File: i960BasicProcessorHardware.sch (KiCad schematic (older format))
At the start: 70 parts, among them J10 Conn_01x03, J11 Conn_01x08, J2 Conn_02x39_Odd_Even, J3 Conn_01x03, J4 Conn_02x05_Odd_Even, J5 Conn_02x05_Odd_Even, J6 Conn_02x05_Odd_Even, J7 Conn_01x06, J8 Conn_01x06, SW1 SW_Push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

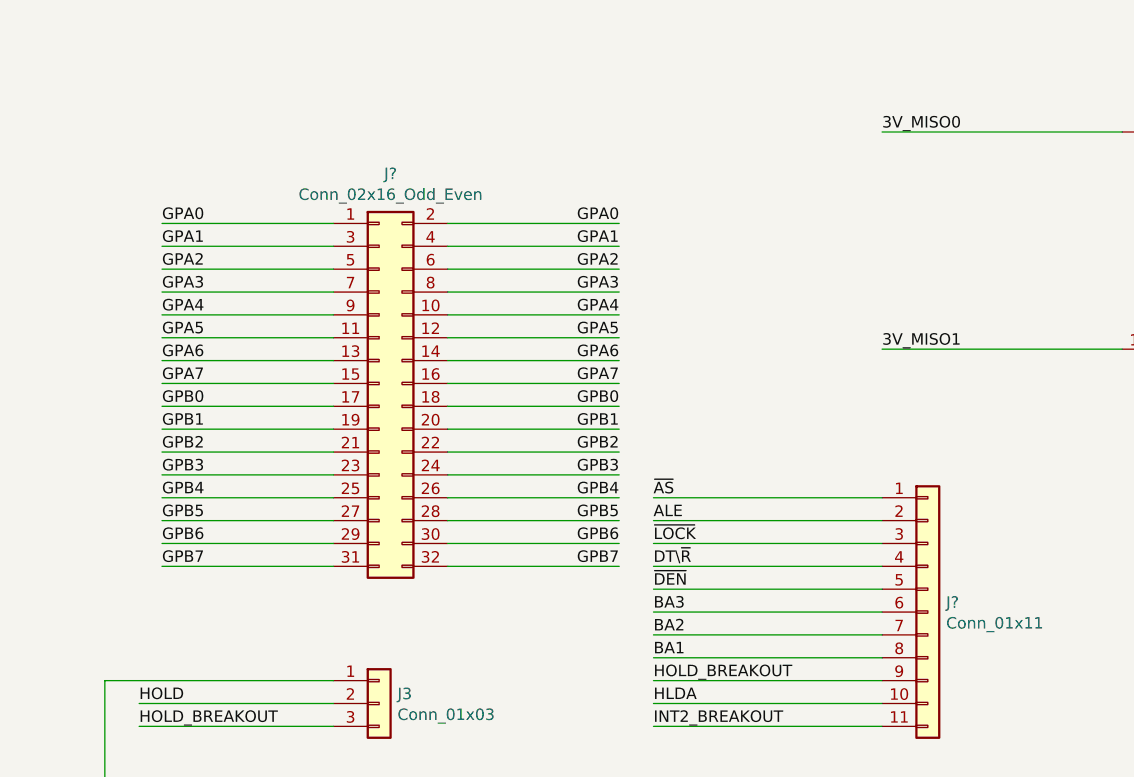
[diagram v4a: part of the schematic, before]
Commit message: Wireup the fourth gpio expander
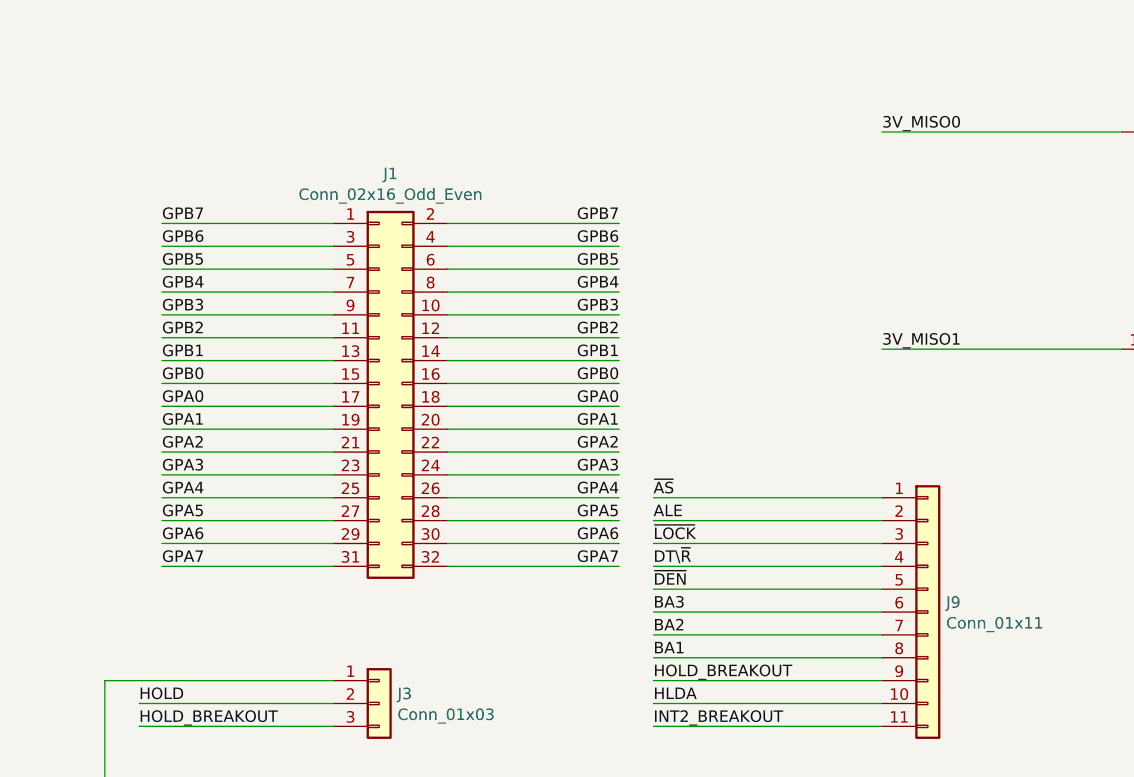
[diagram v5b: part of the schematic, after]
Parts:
- J1: renamed from J?; footprint (none) -> Connector_PinHeader_2.54mm:PinHeader_2x16_P2.54mm_Vertical
- J9: renamed from J?; footprint (none) -> Connector_PinHeader_2.54mm:PinHeader_1x11_P2.54mm_Vertical
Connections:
- net GPA0: now also J1.17 (Pin_17), J1.18 (Pin_18); no longer J1.1 (Pin_1), J1.2 (Pin_2)
- net GPA1: now also J1.19 (Pin_19), J1.20 (Pin_20); no longer J1.3 (Pin_3), J1.4 (Pin_4)
- net GPA2: now also J1.21 (Pin_21), J1.22 (Pin_22); no longer J1.5 (Pin_5), J1.6 (Pin_6)
- net GPA3: now also J1.23 (Pin_23), J1.24 (Pin_24); no longer J1.7 (Pin_7), J1.8 (Pin_8)
- net GPA4: now also J1.25 (Pin_25), J1.26 (Pin_26); no longer J1.10 (Pin_10), J1.9 (Pin_9)
- net GPA5: now also J1.27 (Pin_27), J1.28 (Pin_28); no longer J1.11 (Pin_11), J1.12 (Pin_12)
- net GPA6: now also J1.29 (Pin_29), J1.30 (Pin_30); no longer J1.13 (Pin_13), J1.14 (Pin_14)
- net GPA7: now also J1.31 (Pin_31), J1.32 (Pin_32); no longer J1.15 (Pin_15), J1.16 (Pin_16)
- net GPB0: now also J1.15 (Pin_15), J1.16 (Pin_16); no longer J1.17 (Pin_17), J1.18 (Pin_18)
- net GPB1: now also J1.13 (Pin_13), J1.14 (Pin_14); no longer J1.19 (Pin_19), J1.20 (Pin_20)
- net GPB2: now also J1.11 (Pin_11), J1.12 (Pin_12); no longer J1.21 (Pin_21), J1.22 (Pin_22)
- net GPB3: now also J1.10 (Pin_10), J1.9 (Pin_9); no longer J1.23 (Pin_23), J1.24 (Pin_24)
- net GPB4: now also J1.7 (Pin_7), J1.8 (Pin_8); no longer J1.25 (Pin_25), J1.26 (Pin_26)
- net GPB5: now also J1.5 (Pin_5), J1.6 (Pin_6); no longer J1.27 (Pin_27), J1.28 (Pin_28)
- net GPB6: now also J1.3 (Pin_3), J1.4 (Pin_4); no longer J1.29 (Pin_29), J1.30 (Pin_30)
- net GPB7: now also J1.1 (Pin_1), J1.2 (Pin_2); no longer J1.31 (Pin_31), J1.32 (Pin_32)
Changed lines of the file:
@@
 	19200 17300 18200 17300
 Wire Wire Line
-	16800 15800 16050 15800
-Wire Wire Line
-	16800 15900 16050 15900
-Wire Wire Line
-	16800 16000 16050 16000
-Wire Wire Line
-	16800 16100 16050 16100
-Wire Wire Line
-	16800 16200 16050 16200
-Wire Wire Line
-	16800 16300 16050 16300
-Wire Wire Line
-	16800 16400 16050 16400
-Wire Wire Line
-	16800 16500 16050 16500
+	16800 16600 16050 16600
+Wire Wire Line
+	16800 16700 16050 16700
+Wire Wire Line
+	16800 16800 16050 16800
+Wire Wire Line
+	16800 16900 16050 16900
+Wire Wire Line
+	16800 17000 16050 17000
+Wire Wire Line
+	16800 17100 16050 17100
+Wire Wire Line
+	16800 17200 16050 17200
+Wire Wire Line
+	16800 17300 16050 17300
 Wire Wire Line
 	9000 7850 7650 7850
@@
 Text Label 21450 13750 1    50   ~ 0
 ~RESET960
-Text Label 16050 15800 0    50   ~ 0
+Text Label 16050 16600 0    50   ~ 0
 GPA0
-Text Label 16050 15900 0    50   ~ 0
+Text Label 16050 16700 0    50   ~ 0
 GPA1
-Text Label 16050 16000 0    50   ~ 0
+Text Label 16050 16800 0    50   ~ 0
 GPA2
-Text Label 16050 16100 0    50   ~ 0
+Text Label 16050 16900 0    50   ~ 0
 GPA3
-Text Label 16050 16200 0    50   ~ 0
+Text Label 16050 17000 0    50   ~ 0
 GPA4
-Text Label 16050 16300 0    50   ~ 0
+Text Label 16050 17100 0    50   ~ 0
 GPA5
-Text Label 16050 16400 0    50   ~ 0
+Text Label 16050 17200 0    50   ~ 0
 GPA6
-Text Label 16050 16500 0    50   ~ 0
+Text Label 16050 17300 0    50   ~ 0
 GPA7
 Text Label 14900 16600 2    50   ~ 0
@@
 NoConn ~ 28000 21350
 Wire Wire Line
-	16800 16600 16050 16600
-Wire Wire Line
-	16800 16700 16050 16700
-Wire Wire Line
-	16800 16800 16050 16800
-Wire Wire Line
-	16800 16900 16050 16900
-Wire Wire Line
-	16800 17000 16050 17000
-Wire Wire Line
-	16800 17100 16050 17100
-Wire Wire Line
-	16800 17200 16050 17200
-Wire Wire Line
-	16800 17300 16050 17300
+	16800 16500 16050 16500
+Wire Wire Line
+	16800 16400 16050 16400
+Wire Wire Line
+	16800 16300 16050 16300
+Wire Wire Line
+	16800 16200 16050 16200
+Wire Wire Line
+	16800 16100 16050 16100
+Wire Wire Line
+	16800 16000 16050 16000
+Wire Wire Line
+	16800 15900 16050 15900
+Wire Wire Line
+	16800 15800 16050 15800
 Text Label 31450 3450 2    50   ~ 0
 ~RESET960
@@
 Text Label 14900 16400 2    50   ~ 0
 GPB7
-Text Label 16050 16600 0    50   ~ 0
+Text Label 16050 16500 0    50   ~ 0
 GPB0
-Text Label 16050 16700 0    50   ~ 0
+Text Label 16050 16400 0    50   ~ 0
 GPB1
-Text Label 16050 16800 0    50   ~ 0
+Text Label 16050 16300 0    50   ~ 0
 GPB2
-Text Label 16050 16900 0    50   ~ 0
+Text Label 16050 16200 0    50   ~ 0
 GPB3
-Text Label 16050 17000 0    50   ~ 0
+Text Label 16050 16100 0    50   ~ 0
 GPB4
-Text Label 16050 17100 0    50   ~ 0
+Text Label 16050 16000 0    50   ~ 0
 GPB5
-Text Label 16050 17200 0    50   ~ 0
+Text Label 16050 15900 0    50   ~ 0
 GPB6
-Text Label 16050 17300 0    50   ~ 0
+Text Label 16050 15800 0    50   ~ 0
 GPB7
 $Comp
-L Connector_Generic:Conn_02x16_Odd_Even J?
+L Connector_Generic:Conn_02x16_Odd_Even J1
 U 1 1 79DF032E
 P 17000 16500
-F 0 "J?" H 17050 17417 50  0000 C CNN
+F 0 "J1" H 17050 17417 50  0000 C CNN
 F 1 "Conn_02x16_Odd_Even" H 17050 17326 50  0000 C CNN
-F 2 "" H 17000 16500 50  0001 C CNN
+F 2 "Connector_PinHeader_2.54mm:PinHeader_2x16_P2.54mm_Vertical" H 17000 16500 50  0001 C CNN
 F 3 "~" H 17000 16500 50  0001 C CNN
 	1    17000 16500
@@
 $EndComp
 Wire Wire Line
-	17300 15800 18050 15800
-Wire Wire Line
-	17300 15900 18050 15900
-Wire Wire Line
-	17300 16000 18050 16000
-Wire Wire Line
-	17300 16100 18050 16100
-Wire Wire Line
-	17300 16200 18050 16200
-Wire Wire Line
-	17300 16300 18050 16300
-Wire Wire Line
-	17300 16400 18050 16400
-Wire Wire Line
-	17300 16500 18050 16500
-Text Label 18050 15800 2    50   ~ 0
-GPA0
-Text Label 18050 15900 2    50   ~ 0
-GPA1
-Text Label 18050 16000 2    50   ~ 0
-GPA2
-Text Label 18050 16100 2    50   ~ 0
-GPA3
-Text Label 18050 16200 2    50   ~ 0
-GPA4
-Text Label 18050 16300 2    50   ~ 0
-GPA5
-Text Label 18050 16400 2    50   ~ 0
-GPA6
-Text Label 18050 16500 2    50   ~ 0
-GPA7
-Wire Wire Line
 	17300 16600 18050 16600
 Wire Wire Line
@@
 	17300 17300 18050 17300
 Text Label 18050 16600 2    50   ~ 0
+GPA0
+Text Label 18050 16700 2    50   ~ 0
+GPA1
+Text Label 18050 16800 2    50   ~ 0
+GPA2
+Text Label 18050 16900 2    50   ~ 0
+GPA3
+Text Label 18050 17000 2    50   ~ 0
+GPA4
+Text Label 18050 17100 2    50   ~ 0
+GPA5
+Text Label 18050 17200 2    50   ~ 0
+GPA6
+Text Label 18050 17300 2    50   ~ 0
+GPA7
+Wire Wire Line
+	17300 16500 18050 16500
+Wire Wire Line
+	17300 16400 18050 16400
+Wire Wire Line
+	17300 16300 18050 16300
+Wire Wire Line
+	17300 16200 18050 16200
+Wire Wire Line
+	17300 16100 18050 16100
+Wire Wire Line
+	17300 16000 18050 16000
+Wire Wire Line
+	17300 15900 18050 15900
+Wire Wire Line
+	17300 15800 18050 15800
+Text Label 18050 16500 2    50   ~ 0
 GPB0
-Text Label 18050 16700 2    50   ~ 0
+Text Label 18050 16400 2    50   ~ 0
 GPB1
-Text Label 18050 16800 2    50   ~ 0
+Text Label 18050 16300 2    50   ~ 0
 GPB2
-Text Label 18050 16900 2    50   ~ 0
+Text Label 18050 16200 2    50   ~ 0
 GPB3
-Text Label 18050 17000 2    50   ~ 0
+Text Label 18050 16100 2    50   ~ 0
 GPB4
-Text Label 18050 17100 2    50   ~ 0
+Text Label 18050 16000 2    50   ~ 0
 GPB5
-Text Label 18050 17200 2    50   ~ 0
+Text Label 18050 15900 2    50   ~ 0
 GPB6
-Text Label 18050 17300 2    50   ~ 0
+Text Label 18050 15800 2    50   ~ 0
 GPB7
 $Comp
-L Connector_Generic:Conn_01x11 J?
+L Connector_Generic:Conn_01x11 J9
 U 1 1 79F7F59B
 P 19400 17500
-F 0 "J?" H 19480 17542 50  0000 L CNN
+F 0 "J9" H 19480 17542 50  0000 L CNN
 F 1 "Conn_01x11" H 19480 17451 50  0000 L CNN
-F 2 "" H 19400 17500 50  0001 C CNN
+F 2 "Connector_PinHeader_2.54mm:PinHeader_1x11_P2.54mm_Vertical" H 19400 17500 50  0001 C CNN
 F 3 "~" H 19400 17500 50  0001 C CNN
 	1    19400 17500

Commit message: Drop the attiny85 because I'm going to put several extra attiny861s in its place
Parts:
- removed C27: 0.1uF, Capacitor_SMD:C_0805_2012Metric_Pad1.18x1.45mm_HandSolder, symbol Device:C
- removed J8: Conn_01x06, Connector_PinHeader_2.54mm:PinHeader_1x06_P2.54mm_Vertical, symbol Connector_Generic:Conn_01x06
- removed SW1: SW_Push, Button_Switch_THT:SW_PUSH_6mm_H4.3mm, symbol Switch:SW_Push
- removed U18: ATtiny85-20PU, Package_DIP:DIP-8_W7.62mm_Socket, symbol MCU_Microchip_ATtiny:ATtiny85-20PU
- added C? (x2): 0.1uF, Capacitor_SMD:C_0805_2012Metric_Pad1.18x1.45mm_HandSolder, symbol Device:C
- added U?: ATtiny861-20PU, Package_DIP:DIP-20_W7.62mm, symbol MCU_Microchip_ATtiny:ATtiny861-20PU
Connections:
- net +5V: now also C?.1, C?.1, U?.15 (AVCC), U?.5 (VCC)
- net CLKO: now also U?.7 (XTAL1/PB4)
- net GND: now also C?.2, C?.2, U?.16 (AGND), U?.6 (GND), U?.8 (XTAL2/PB5)
- net ~MCU_RESET: now also U?.10 (~RESET~/PB7)
- new net AVR861_INT0: U?.9 (PB6)
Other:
- moved on the sheet: B1, J4, J5, J6, J7

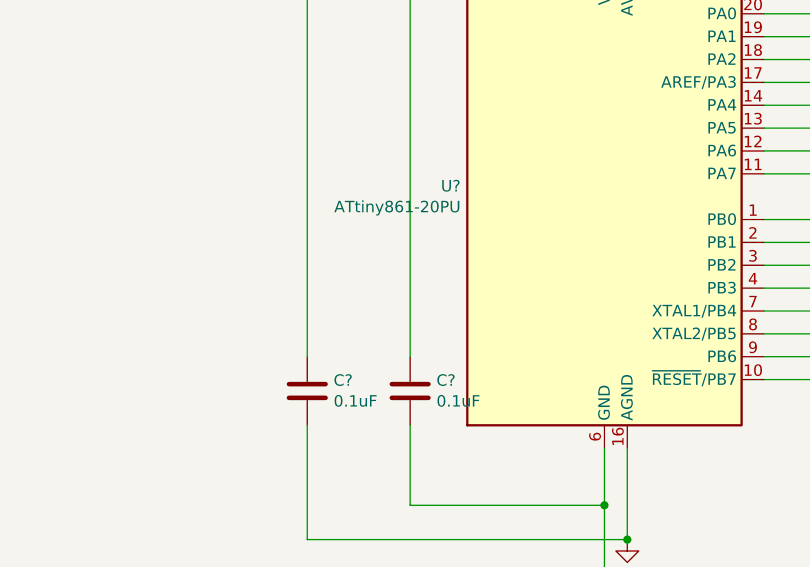
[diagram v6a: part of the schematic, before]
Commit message: Drop the attiny85
I am going to place two 861s instead tied to the same 20mhz clock

I am also considering adding a dip40 socket also tied to the same
20mhz clock
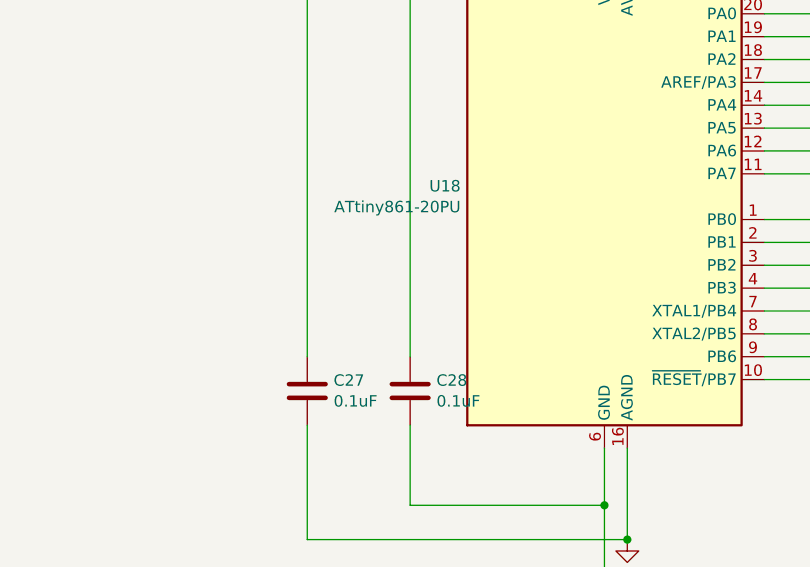
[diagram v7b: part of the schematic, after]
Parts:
- gave numbers to parts that had none: 3
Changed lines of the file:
@@
 $EndComp
 $Comp
-L MCU_Microchip_ATtiny:ATtiny861-20PU U?
+L MCU_Microchip_ATtiny:ATtiny861-20PU U18
 U 1 1 7A5F676E
 P 22700 2750
-F 0 "U?" H 22071 2796 50  0000 R CNN
+F 0 "U18" H 22071 2796 50  0000 R CNN
 F 1 "ATtiny861-20PU" H 22071 2705 50  0000 R CNN
 F 2 "Package_DIP:DIP-20_W7.62mm" H 22700 2750 50  0001 C CIN
@@
 	22700 4100 22700 3850
 $Comp
-L Device:C C?
+L Device:C C28
 U 1 1 7A6C09AB
 P 21850 3600
-F 0 "C?" H 21965 3646 50  0000 L CNN
+F 0 "C28" H 21965 3646 50  0000 L CNN
 F 1 "0.1uF" H 21965 3555 50  0000 L CNN
 F 2 "Capacitor_SMD:C_0805_2012Metric_Pad1.18x1.45mm_HandSolder" H 21888 3450 50  0001 C CNN
@@
 	21850 3750 21850 4100
 $Comp
-L Device:C C?
+L Device:C C27
 U 1 1 7A6C1395
 P 21400 3600
-F 0 "C?" H 21515 3646 50  0000 L CNN
+F 0 "C27" H 21515 3646 50  0000 L CNN
 F 1 "0.1uF" H 21515 3555 50  0000 L CNN
 F 2 "Capacitor_SMD:C_0805_2012Metric_Pad1.18x1.45mm_HandSolder" H 21438 3450 50  0001 C CNN
@@
 Connection ~ 22700 4100
 $Comp
-L power:GND #PWR?
+L power:GND #PWR0104
 U 1 1 7A91E3FB
 P 22700 4550
-F 0 "#PWR?" H 22700 4300 50  0001 C CNN
+F 0 "#PWR0104" H 22700 4300 50  0001 C CNN
 F 1 "GND" H 22705 4377 50  0000 C CNN
 F 2 "" H 22700 4550 50  0001 C CNN
@@
 $EndComp
 $Comp
-L power:GND #PWR?
+L power:GND #PWR0105
 U 1 1 7A91E440
 P 22800 4250
-F 0 "#PWR?" H 22800 4000 50  0001 C CNN
+F 0 "#PWR0105" H 22800 4000 50  0001 C CNN
 F 1 "GND" H 22805 4077 50  0000 C CNN
 F 2 "" H 22800 4250 50  0001 C CNN
@@
 P 22700 950
 AR Path="/640CD6D6/7AAB2892" Ref="#PWR?"  Part="1"
-AR Path="/7AAB2892" Ref="#PWR?"  Part="1"
-F 0 "#PWR?" H 22700 800 50  0001 C CNN
+AR Path="/7AAB2892" Ref="#PWR0106"  Part="1"
+F 0 "#PWR0106" H 22700 800 50  0001 C CNN
 F 1 "+5V" H 22715 1123 50  0000 C CNN
 F 2 "" H 22700 950 50  0001 C CNN
@@
 P 23000 950
 AR Path="/640CD6D6/7AAB2CAF" Ref="#PWR?"  Part="1"
-AR Path="/7AAB2CAF" Ref="#PWR?"  Part="1"
-F 0 "#PWR?" H 23000 800 50  0001 C CNN
+AR Path="/7AAB2CAF" Ref="#PWR0107"  Part="1"
+F 0 "#PWR0107" H 23000 800 50  0001 C CNN
 F 1 "+5V" H 23015 1123 50  0000 C CNN
 F 2 "" H 23000 950 50  0001 C CNN
@@
 	23400 3350 24500 3350
 $Comp
-L power:GND #PWR?
+L power:GND #PWR0108
 U 1 1 7B4FE180
 P 24500 4100
-F 0 "#PWR?" H 24500 3850 50  0001 C CNN
+F 0 "#PWR0108" H 24500 3850 50  0001 C CNN
 F 1 "GND" H 24505 3927 50  0000 C CNN
 F 2 "" H 24500 4100 50  0001 C CNN
